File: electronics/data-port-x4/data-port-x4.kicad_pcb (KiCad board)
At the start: 4 copper layers, 108 x 24 mm, 95 parts, among them J1 LEAD, J101 PORT1, J102 AUX1, J201 PORT2, J202 AUX2, J301 PORT3, J302 AUX3, J401 PORT4, J402 AUX4, U1 USB2514B-AEZC-TR, U101 TPS2553DBVR-1, U102 INA226AIDGSR, U103 USBLC6-2SC6, U2 TCA6408ARGTR, U201 TPS2553DBVR-1, U202 INA226AIDGSR, U203 USBLC6-2SC6, U3 AP2112K-3.3TRG1, U301 TPS2553DBVR-1, U302 INA226AIDGSR, U303 USBLC6-2SC6, U4 USBLC6-2SC6, U401 TPS2553DBVR-1, U402 INA226AIDGSR, U403 USBLC6-2SC6, U5 USBLC6-2SC6, U6 TCA6408ARGTR, Y1 X322524MSB4SI

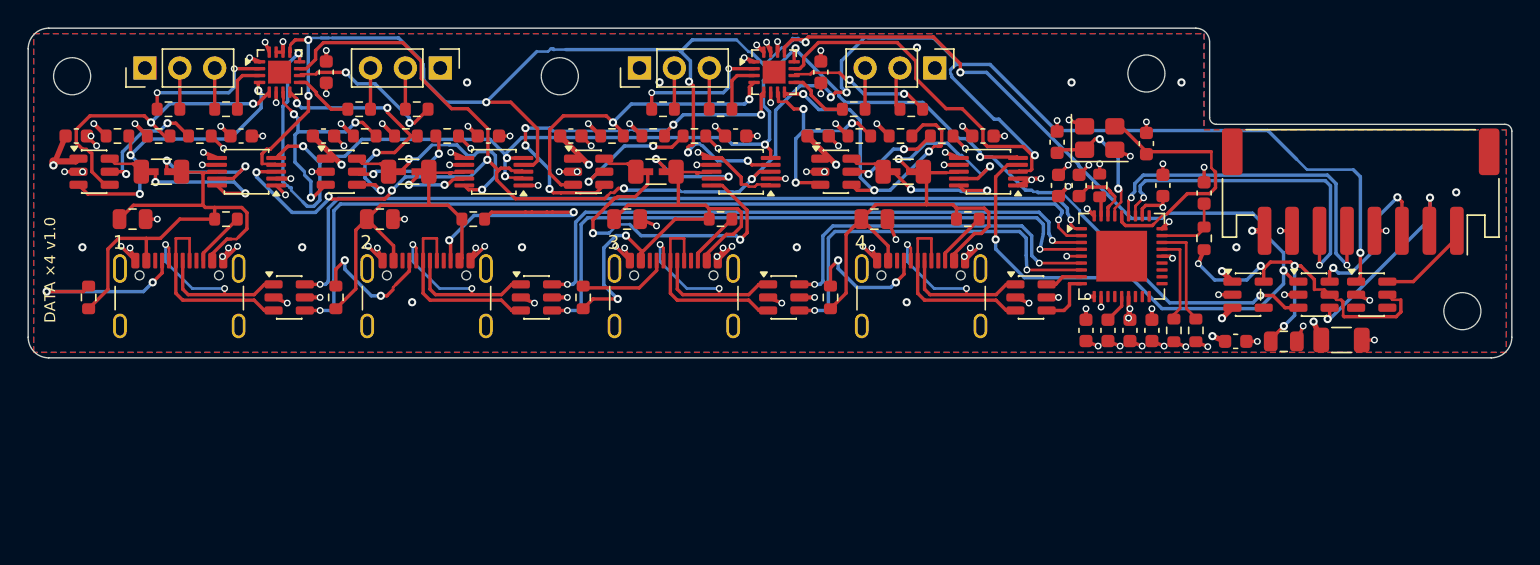
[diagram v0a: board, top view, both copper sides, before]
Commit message: DATA ×4: the lead's D+/D− follow J7, the upstream pair rerouted
The node's J7 now has D+ on pin 3 and D− on pin 4 (094341c); the lead
mirrors pins (n ↔ 9 − n), so J1 takes D− on pin 5 and D+ on pin 6, like
the single DATA port's J2.  The upstream pair is drawn again without a
crossover: two vias in front of J1 (D+ north of D−), B.Cu west, north
along x 87 (clear of In2's +3V3 edge), west and south into the hub's top
pins; every turn keeps D+ on the pair's right, west of D− at the hub.

The new route moved the router's vias, and two of them cut In2's +5V in
half under the hub's capacitors: the +3V3 tab there ends at y 21.6 and a
via-only keep-out (pcbgen keepouts "vias_only") keeps the 1.9 mm +5V neck
whole.  The 22 µF VBUS caps' LCSC/MPN fields now reach the schematic and
the PCB too.  Docs: the lead pinout row.

ERC 0, DRC 0 (unconnected 0, parity 0); Konnect: 0 errors, the same three
library-copy warnings, JLC DFM 0.

Co-Authored-By: Claude Opus 5.5 <noreply@anthropic.com>
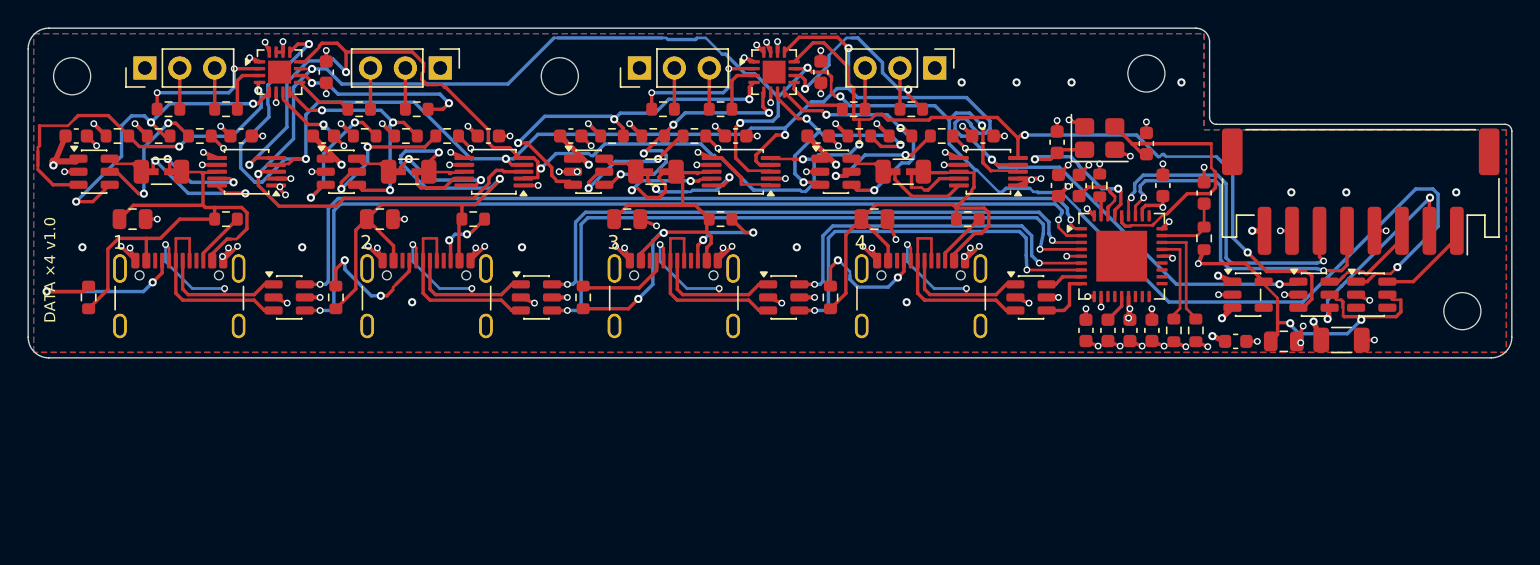
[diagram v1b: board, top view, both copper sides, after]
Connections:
- J1 pad 5: /Hub/UP_DP -> /Hub/UP_DN
- J1 pad 6: /Hub/UP_DN -> /Hub/UP_DP
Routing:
- net SDA: track 158.7 -> 130.0 mm, vias 10 -> 7
- net /Port 2/PORT2_VBUS: track 27.3 -> 42.6 mm, vias 0 -> 2
- net /Port 3/PORT3_SNS_P: track 24.1 -> 8.99 mm
- net /Port 2/PORT2_CC2: track 18.3 -> 4.73 mm
- net SCL: track 118.3 -> 129.9 mm, vias 8 -> 7
- net PORT3_FLT_N: track 30.1 -> 19.7 mm, vias 5 -> 4
- net /Port 4/PORT4_SNS_N: track 12.3 -> 5.02 mm, vias 2 -> 0
- net /Port 3/PORT3_VBUS: track 37.8 -> 32.2 mm
- net INT: track 167.7 -> 162.4 mm, vias 10 -> 7
- net PORT1_EN: track 22.2 -> 27.2 mm, vias 3 -> 2
- net PORT4_FLT_N: track 23.8 -> 18.8 mm
- net /Hub/LEAD_SDA: track 12.1 -> 7.24 mm, vias 2 -> 0
- net /Port 2/PORT2_SNS_P: track 12.8 -> 8.43 mm
- net PORT4_RST_IO: track 10.6 -> 14.9 mm
- net PORT4_EN: track 15.7 -> 19.3 mm
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
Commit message: DATA ×4: a basic-part LDO, the XC6206 in U3's spot
U3 goes from the AP2112K-3.3 (extended) to the XC6206P332MR-G (C5446,
JLC basic, SOT-23-3): one extended part type fewer, $3.07 an order at
Economic PCBA.  Its dropout is ≈ 0.25 V at 0.1 A against the board's
≈ 0.1 A of logic, so the hub, the expanders and the INA226s still run
down to ≈ 3.6 V in; 200 mA max, 6 V in max (the node's +5V is 5.24 V).
The AMS1117 suggested first doesn't fit (SOT-223 under J1) and its ≈ 1 V
dropout would eat the lead's margin.  U3 sits at 0° (of three
orientations routed, the one Freerouting closed), CPL fix 180° for
C5446.

Re-routed: ERC 0, DRC 0 (unconnected 0, parity 0).  BOM: the DATA ×4
quote at 8 extended types ($74.44), its lever moves out of JLC_LEVERS.

Co-Authored-By: Claude Opus 5.5 <noreply@anthropic.com>
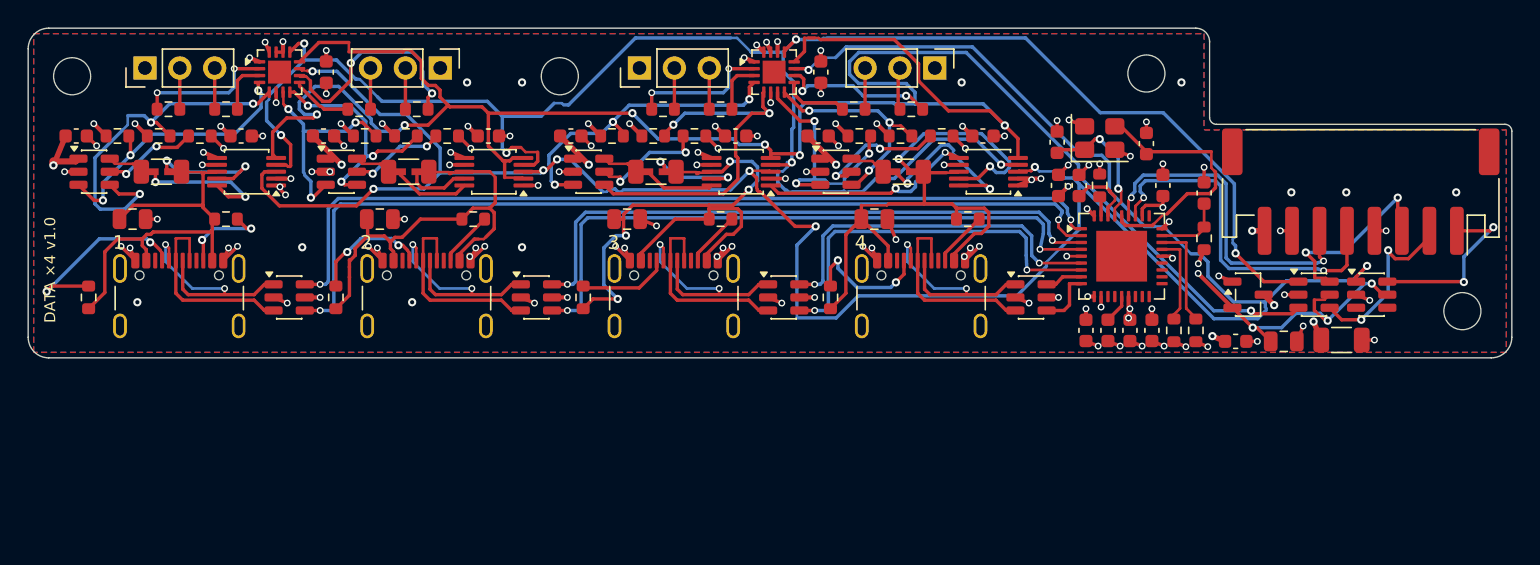
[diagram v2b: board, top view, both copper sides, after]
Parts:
- U3: value AP2112K-3.3TRG1 -> XC6206P332MR-G; footprint Package_TO_SOT_SMD:SOT-23-5 -> Package_TO_SOT_SMD:SOT-23-3
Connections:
- U3 pad 1: +5V -> GND
- U3 pad 2: GND -> +3V3
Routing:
- net SCL: track 129.9 -> 162.3 mm
- net INT: track 162.4 -> 177.9 mm, vias 7 -> 9
- net /Port 3/PORT3_VBUS: track 32.2 -> 44.5 mm, vias 2 -> 4
- net SDA: track 130.0 -> 142.0 mm
- net /Port 4/PORT4_SNS_N: track 5.02 -> 15.8 mm, vias 0 -> 2
- net /Port 2/PORT2_VBUS: track 42.6 -> 32.1 mm, vias 2 -> 0
- net PORT3_FLT_N: track 19.7 -> 27.3 mm, vias 4 -> 2
- net /Hub/LEAD_SDA: track 7.24 -> 14.2 mm, vias 0 -> 2
- net /Port 4/PORT4_SNS_P: track 6.05 -> 12.6 mm, vias 0 -> 2
- net PORT1_EN: track 27.2 -> 20.7 mm, vias 2 -> 3
- net /Hub/LEAD_INT: track 6.90 -> 13.2 mm, vias 0 -> 2
- net +3V3: track 73.4 -> 79.1 mm, vias 41 -> 44
- net /Port 1/PORT1_VBUS: track 36.0 -> 30.8 mm
- net PORT3_EN: track 26.9 -> 22.7 mm
- net /Port 2/PORT2_ILIM: track 11.1 -> 6.99 mm
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
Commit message: DATA ×4: back to the AP2112K on U3, on top-side copper
The XC6206 (82c7172) can't carry this rail.  The USB2514B alone draws up
to 155 mA at high speed with four ports busy (datasheet tables 6-4 and
6-5; 84 mA at full speed), so the LDO burns ≈ 0.31 W from 5.24 V: more
than a 200 mA SOT-23 LDO like the XC6206 is rated for (≈ 0.25 W), and the
XC6206 has no thermal shutdown.  The AP2112K-3.3 (600 mA, thermal
shutdown) is back on its SOT-23-5 footprint at 0°, CPL 270° as before;
C5446 and its catalog entry go.

Its VIN and EN pins (with C2's +5V pad) and its GND pin now sit on
top-side islands (exclusive, thermal reliefs) with their own vias to the
+5V and GND planes, to spread that heat.  design.py and docs/electronics.md
say why, so it isn't swapped again.

Re-routed: ERC 0, DRC 0 (unconnected 0, parity 0).  BOM: back to 9
extended types, the DATA ×4 order $103.76.

Co-Authored-By: Claude Opus 5.5 <noreply@anthropic.com>
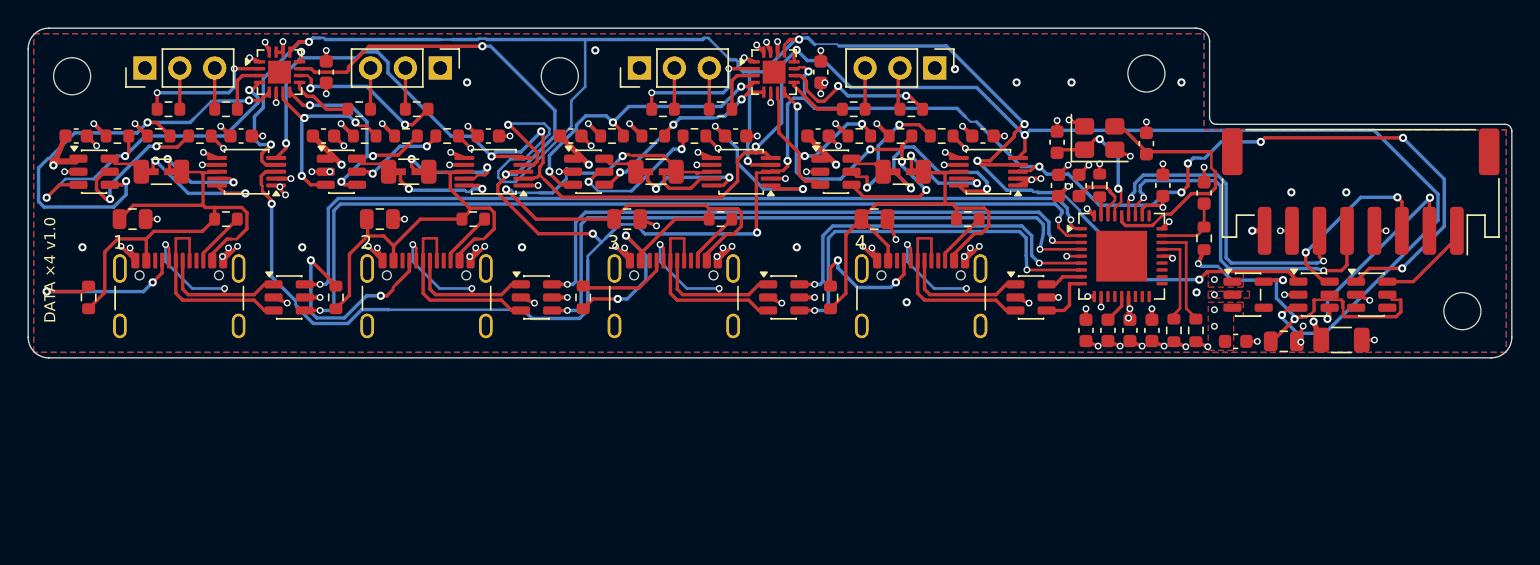
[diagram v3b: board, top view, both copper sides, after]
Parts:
- U3: value XC6206P332MR-G -> AP2112K-3.3TRG1; footprint Package_TO_SOT_SMD:SOT-23-3 -> Package_TO_SOT_SMD:SOT-23-5
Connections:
- U3 pad 1: GND -> +5V
- U3 pad 2: +3V3 -> GND
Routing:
- net SCL: track 162.3 -> 139.9 mm, vias 7 -> 8
- net /Port 3/PORT3_VBUS: track 44.5 -> 59.5 mm
- net PORT3_FLT_N: track 27.3 -> 15.6 mm, vias 2 -> 3
- net PORT4_FLT_N: track 16.5 -> 26.0 mm, vias 3 -> 4
- net /Port 4/PORT4_SNS_N: track 15.8 -> 8.27 mm
- net /Port 2/PORT2_CC1: track 8.86 -> 16.0 mm
- net /Hub/LEAD_INT: track 13.2 -> 6.90 mm, vias 2 -> 0
- net PORT1_FLT_N: track 27.0 -> 32.8 mm
- net /Port 1/PORT1_VBUS: track 30.8 -> 36.0 mm
- net /Port 2/PORT2_SNS_N: track 4.71 -> 9.37 mm, vias 0 -> 2
- net PORT2_RST_IO: track 16.4 -> 11.9 mm
- net /Port 1/PORT1_ILIM: track 7.02 -> 11.4 mm
- net PORT1_EN: track 20.7 -> 24.7 mm
- net /Port 3/PORT3_SNS_P: track 5.21 -> 8.81 mm, vias 0 -> 2
- net SDA: track 142.0 -> 145.0 mm, vias 7 -> 8
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- added copper zone on F.Cu, net +5V

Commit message: DATA ×4: the PCBA review's fixes
X2: the lead's SDA, SCL and INT go through three 2N7002 (gate on this
board's +3V3, NXP AN10441) with 4.7k / 4.7k / 10k pull-ups on this side,
and the lead USBLC6s' VBUS pins are open: with DUT_5V off the node's
pull-ups no longer feed the dead board through the INA226 and TCA6408A
clamps.  X3: EN pulled down, every port off until the firmware enables
it.  X4: the Port netclass patterns get their leading *, VBUS and CC are
drawn at each receptacle (0.4 mm, no via on the CC lines), the INA226
reads Vbus on the shunt's sense pad, and R_ILIM sits beside its pin.  X5:
a shallow +3V3 tab and no via in the 2.5 mm +5V neck under the hub; the
bottom row's GND pads go on a bus to a via at each end.  X6: 100k
pull-ups on RESET and BOOT.  X7: TI's 1.45 mm exposed pad for the
TCA6408A.  X8: NON_REM0/1 pulled down.  X9: In2 notches keep the
upstream and PORT1 pairs over +5V all along; 100 nF at each port
USBLC6's VBUS.  X10: the crystal, PLLFILT and RBIAS drawn, no via.  X11
starts a bring-up measurement list in electronics.md.

The CPL audit agrees on all 106 parts (U3 and the new VQFN included).
Freerouting's few-µm dots on pads are dropped at import.  ERC 0, DRC 0,
parity 0, 0 unconnected; the BOM follows (about $104 for 5 with 2
assembled).

Co-Authored-By: Claude Opus 5.5 <noreply@anthropic.com>
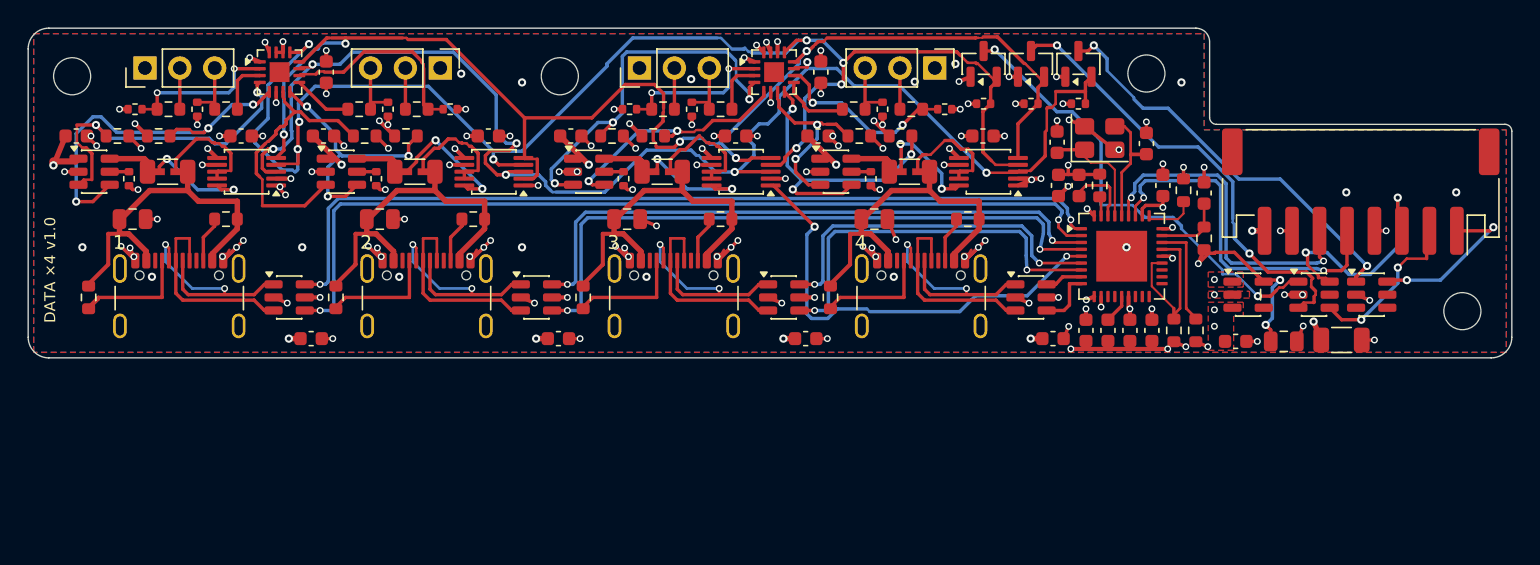
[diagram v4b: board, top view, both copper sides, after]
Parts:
- added C104: 100n, Capacitor_SMD:C_0603_1608Metric, F.Cu at (20.6, 22.6)
- added C204: 100n, Capacitor_SMD:C_0603_1608Metric, F.Cu at (38.6, 22.6)
- added C304: 100n, Capacitor_SMD:C_0603_1608Metric, F.Cu at (56.6, 22.6)
- added C404: 100n, Capacitor_SMD:C_0603_1608Metric, F.Cu at (74.6, 22.6)
- added Q1: 2N7002, Package_TO_SOT_SMD:SOT-23, F.Cu at (69.5, 2.60)
- added Q2: 2N7002, Package_TO_SOT_SMD:SOT-23, F.Cu at (73.0, 2.60)
- added Q3: 2N7002, Package_TO_SOT_SMD:SOT-23, F.Cu at (76.5, 2.60)
- added R109: 100k, Resistor_SMD:R_0402_1005Metric, F.Cu at (7.78, 5.90)
- added R110: 100k, Resistor_SMD:R_0402_1005Metric, F.Cu at (12.3, 5.90)
- added R209: 100k, Resistor_SMD:R_0402_1005Metric, F.Cu at (30.7, 5.90)
- added R210: 100k, Resistor_SMD:R_0402_1005Metric, F.Cu at (26.2, 5.90)
- added R309: 100k, Resistor_SMD:R_0402_1005Metric, F.Cu at (43.8, 5.90)
- added R310: 100k, Resistor_SMD:R_0402_1005Metric, F.Cu at (48.3, 5.90)
- added R409: 100k, Resistor_SMD:R_0402_1005Metric, F.Cu at (66.7, 5.90)
- added R410: 100k, Resistor_SMD:R_0402_1005Metric, F.Cu at (62.2, 5.90)
- added R5: 100k, Resistor_SMD:R_0603_1608Metric, F.Cu at (84.1, 11.8)
- added R6: 4.7k, Resistor_SMD:R_0402_1005Metric, F.Cu at (69.5, 5.50)
- added R7: 4.7k, Resistor_SMD:R_0402_1005Metric, F.Cu at (73.0, 5.50)
- added R8: 10k, Resistor_SMD:R_0402_1005Metric, F.Cu at (76.5, 5.50)
- R101, R201, R301, R401: footprint Resistor_SMD:R_0603_1608Metric -> Resistor_SMD:R_0402_1005Metric
- U2, U6: footprint Package_DFN_QFN:QFN-16-1EP_3x3mm_P0.5mm_EP1.675x1.675mm -> Package_DFN_QFN:VQFN-16-1EP_3x3mm_P0.5mm_EP1.45x1.45mm
- moved R101 6.02 mm to (7.34, 11.0), turned to -90 degrees
- moved R201 6.02 mm to (25.3, 11.0), turned to -90 degrees
- moved R301 6.02 mm to (43.3, 11.0), turned to -90 degrees
- moved R401 6.02 mm to (61.3, 11.0), turned to -90 degrees
- moved R406 0.45 mm to (64.2, 10.4)
- moved R106 0.45 mm to (10.2, 10.4)
- moved R206 0.45 mm to (28.1, 10.4)
- moved R306 0.45 mm to (46.1, 10.4)
- turned R104 to -90 degrees
- turned R105 to 180 degrees
- turned R204 to -90 degrees
- turned R205 to 180 degrees
- turned R304 to -90 degrees
- turned R305 to 180 degrees
- turned R404 to -90 degrees
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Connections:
- R102 pad 1: +3V3 -> PORT1_EN
- R102 pad 2: PORT1_EN -> GND
- R202 pad 1: +3V3 -> PORT2_EN
- R202 pad 2: PORT2_EN -> GND
- R302 pad 1: +3V3 -> PORT3_EN
- R302 pad 2: PORT3_EN -> GND
- R402 pad 1: +3V3 -> PORT4_EN
- R402 pad 2: PORT4_EN -> GND
- U1 pad 22: unconnected-(U1-SDA/SMBDATA/NON_REM1-Pad22) -> /Hub/CFG_SEL0
- U1 pad 28: unconnected-(U1-SUSP_IND/LOCAL_PWR/NON_REM0-Pad28) -> /Hub/NON_REM0
- U102 pad 8: /Port 1/PORT1_VBUS -> /Port 1/PORT1_SNS_N
- U202 pad 8: /Port 2/PORT2_VBUS -> /Port 2/PORT2_SNS_N
- U302 pad 8: /Port 3/PORT3_VBUS -> /Port 3/PORT3_SNS_N
- U4 pad 1: SDA -> /Hub/BUS_SDA
- U4 pad 3: SCL -> /Hub/BUS_SCL
- U4 pad 5: +3V3 -> unconnected-(U4-VBUS-Pad5)
- U402 pad 8: /Port 4/PORT4_VBUS -> /Port 4/PORT4_SNS_N
- U5 pad 1: INT -> /Hub/BUS_INT
- U5 pad 5: +3V3 -> unconnected-(U5-VBUS-Pad5)
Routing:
- net INT: track 175.4 -> 102.7 mm, vias 13 -> 7
- net SCL: track 139.9 -> 99.1 mm, vias 8 -> 5
- net SDA: track 145.0 -> 106.6 mm
- net /Hub/BUS_SDA: track 0.00 -> 33.9 mm, vias 0 -> 2
- net /Port 3/PORT3_VBUS: track 59.5 -> 25.6 mm, vias 4 -> 0
- net /Hub/BUS_SCL: track 0.00 -> 33.3 mm, vias 0 -> 2
- net /Hub/BUS_INT: track 0.00 -> 29.9 mm, vias 0 -> 2
- net GND: track 85.7 -> 113.1 mm, vias 98 -> 110
- net /Port 1/PORT1_VBUS: track 36.0 -> 25.6 mm
- net /Port 1/PORT1_ILIM: track 11.4 -> 1.40 mm, vias 2 -> 0
- net +3V3: track 79.7 -> 89.3 mm, vias 42 -> 51
- net /Port 3/PORT3_ILIM: track 10.8 -> 1.40 mm, vias 2 -> 0
- net /Hub/XO: track 19.2 -> 9.99 mm
- net /Port 4/PORT4_ILIM: track 10.2 -> 1.40 mm, vias 2 -> 0
- net /Port 2/PORT2_CC1: track 16.0 -> 8.44 mm, vias 2 -> 0
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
